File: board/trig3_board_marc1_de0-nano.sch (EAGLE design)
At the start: 305 parts, among them IC1 ICL7660CPA, IC2 ICL7660CPA, IC3 ICL7660CPA, IC4 ICL7660CPA, J10 2p-2.54, J11 2p-2.54, J12 4p-2.54, J13 BU-SMB-V, J131 4p-2.54, J14 BU-SMB-V, J141 2p-2.54, J15 2p-2.54, J16 2p-2.54, J17 2p-2.54, J18 2p-2.54, J19 6HE-160-VG64AC, J20 4p-2.54, J21 4p-2.54, J22 2p-2.54, J23 2p-2.54, J24 2p-2.54, J25 2p-2.54, J26 4p-2.54, J27 4p-2.54, J28 2p-2.54, J29 2p-2.54, J3 4p-2.54, J30 2p-2.54, J31 2p-2.54, J311 4p-2.54, J32 2p-2.54, J33 2p-2.54, J34 2p-2.54, J35 2p-2.54, J36 2p-2.54, J37 2p-2.54, J38 2p-2.54, J39 2p-2.54, J4 2p-2.54, J40 2p-2.54, J41 2p-2.54, J42 2p-2.54, J43 2p-2.54, J48 2p-2.54, J49 2p-2.54, J5 2p-2.54, J50 2p-2.54, J51 2p-2.54, J52 2p-2.54, J53 2p-2.54, J54 2p-2.54, J55 2p-2.54, J6 2p-2.54, J7 4p-2.54, J8 2p-2.54, J9 2p-2.54, K15_R10P BU-SMB-V, K16_R10N BU-SMB-V, M16CLK_3N BU-SMB-V, P11 BU-SMB-V, P14_CLKOUT_4P BU-SMB-V, P15 BU-SMB-V, P16_R15N BU-SMB-V, P9 BU-SMB-V, T10_B16N BU-SMB-V, T12_B18N BU-SMB-V, T13_B20N BU-SMB-V, T14_B23P BU-SMB-V, T15_B23N BU-SMB-V, T9CLK_7N BU-SMB-V

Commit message: slim it down and add usb-serial
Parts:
- removed A12_T21N, A14_CLKOUT_2N, A2_T2N, A3_T2P, A5, A7_T9N, A8CLK_4N, B11, B12_T21P, B16, B5, B7_T9P, B8CLK_4P, C11, C14, C15, C16, C3_CLKOUT_3N, C6, C8, C9_T15N, D11, D14, D15, D16, D3_CLKOUT_3P, D5, D6, D8, D9_T15P, E10, E11, E15CLK_2P, E16CLK_2N, E6, E7, E8_T10N, E9, F14, F15, F16, F8_T10P, F9, G15_R5P, G16_R5N, J13, J14, K15_R10P, K16_R10N, L16_R11N, M16CLK_3N, N12, N14, N15_R13P, N16_R13N, P11, P14_CLKOUT_4P, P15, R10_B16P, R12_B18P, R13_B20P, R14_CLKOUT_4N, T10_B16N, T12_B18N, T13_B20N, T14_B23P, T15_B23N: BU-SMB-V, con-coax:BU-SMB-V
- removed C1, C12, C13, C17, C18, C3, C7, C9: 10uF, SparkFun-Capacitors:CAPPTH1
- removed C19, C2, C20, C21, C22, C4, C5, C91, C93, C94, C95, C97: 0.1uF, SparkFun-Capacitors:CAP0805
- removed IC1, IC2, IC3, IC4: ICL7660CPA, maxim:ICL7660CPA
- removed J1, J2: (no value), SparkFun-Connectors:M13X22X13
- removed J10, J11, J141, J15, J16, J17, J18, J22, J23, J24, J25, J28, J29, J30, J31, J32, J33, J35, J36, J37, J38, J39, J4, J40, J41, J48, J49, J50, J51, J52, J53, J54, J55, J8, J9, OJ1, OJ10, OJ11, OJ12, OJ17, OJ18, OJ19, OJ2, OJ20, OJ21, OJ22, OJ23, OJ24, OJ25, OJ26, OJ27, OJ28, OJ29, OJ3, OJ30, OJ31, OJ32, OJ33, OJ34, OJ35, OJ36, OJ37, OJ38, OJ39, OJ4, OJ40, OJ49, OJ5, OJ50, OJ51, OJ52, OJ53, OJ54, OJ55, OJ56, OJ57, OJ58, OJ59, OJ6, OJ60, OJ61, OJ62, OJ63, OJ64, OJ65, OJ66, OJ67, OJ68, OJ69, OJ7, OJ70, OJ71, OJ72, OJ73, OJ74, OJ75, OJ76, OJ77, OJ78, OJ79, OJ8, OJ80, OJ9: 2p-2.54, Seeed-Connector:DIP-BLACK-MALE-HEADER-VERT(2P-2.54)
- removed J131, J311: 4p-2.54, Seeed-Connector:DIP-BLACK-FEMALE-HEADER-VERT(4P-2.54)
- removed J19: 6HE-160-VG64AC, 19inch:6HE-160-VG64AC
- removed J20, J21, J26, J27: 4p-2.54, Seeed-Connector:DIP-BLACK-MALE-HEADER-VERT(4P-2.54)
- removed R10, R12, R13, R14: 1k, SparkFun-Passives:RESISTORAXIAL-0.3
- removed R100, R11, R111, R141, R15, R161, R18, R19, R20, R21, R22, R23, R24, R25, R26, R27, R28, R29, R30, R32, R33, R35, R39, R4, R40, R45, R46, R47, R49, R50, R51, R52, R53, R9, R91: 50, SparkFun-Passives:RESISTORAXIAL-0.3
- removed R17: 10k, SparkFun-Passives:RESISTORAXIAL-0.3
- removed R2, R3, R7: 3296W 5k, resistor:R-TRIMM3296W
- removed VSLUE, VSLUE2, VSLUE3, VSLUE4, VSLUE6, VSLUE7, VSLUE8, VSLUE9: SN74ACT244DW, SN74ACT244DW:SN74ACT244DW
- added C_OSC1, C_OSC2: 22pF, rcl@1:C-USC0603
- added U340G: CH340G, usb-serial:CH340G
- added USB1: MF-CON-MICROUSB-RIGHT, PP_Connectors:USB_5PIN_10118193-0001LF
- added Y1: ABL-12.000MHZ-B2, SparkFun-FreqCtrl:CRYSTALHC49US
- R1: value 3296W 5k -> 10k; device resistor:R-TRIMM3296W -> adafruit:R-US_R0805
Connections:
- removed net -3V3_1: C3.1, IC1.VOUT, J20.P$1, R10.2
- removed net -3V3_2: C9.1, IC2.VOUT, J21.P$1, R12.2
- removed net -3V3_3: C13.1, IC3.VOUT, J26.P$1, R13.2
- removed net -3V3_4: C18.1, IC4.VOUT, J27.P$1, R14.2
- removed net -V1: C19.2, J20.P$2, OJ9.1, R1.S
- removed net -V2: C20.2, J21.P$2, OJ10.1, R2.S
- removed net -V3: C21.2, J26.P$2, OJ11.1, R3.S
- removed net -V4: C22.2, J27.P$2, OJ12.1, R7.S
- removed net AIN0: J1.24, J131.P$4
- removed net AIN1: J1.25, J311.P$1
- removed net AIN2: J1.22, J131.P$3
- removed net AIN3: J1.21, J311.P$3
- removed net AIN4: J1.23, J311.P$2
- removed net AIN5: J1.18, J131.P$1
- removed net AIN6: J1.19, J311.P$4
- removed net AIN7: J1.20, J131.P$2
- removed net GPIO_018_E7: OJ64.1, SV1.23, VSLUE7.1A3, VSLUE7.1A4
- removed net GPIO_019_D8: OJ21.1, SV1.24, VSLUE2.2A3, VSLUE2.2A4
- removed net GPIO_01_C3: C3_CLKOUT_3N.1, J30.2, R27.2, SV1.4
- removed net GPIO_021_F8: F8_T10P.1, J18.2, R21.2, SV1.26
- removed net GPIO_022_F9: OJ62.1, SV1.27, VSLUE7.2A1, VSLUE7.2A2
- removed net GPIO_023_E9: OJ24.1, SV1.28, VSLUE2.1A3, VSLUE2.1A4
- removed net GPIO_112_N12: OJ23.1, SV2.17, VSLUE2.1A1, VSLUE2.1A2
- removed net GPIO_120_P15: OJ61.1, SV2.25, VSLUE7.2A3, VSLUE7.2A4
- removed net GPIO_20_A14: A14_CLKOUT_2N.1, J1.5, J31.2, R29.2
- removed net GPIO_210_F14: J1.15, OJ30.1, VSLUE3.2A1, VSLUE3.2A2
- removed net GPIO_211_G16: G16_R5N.1, J1.16, J28.2, R24.2
- removed net GPIO_212_G15: G15_R5P.1, J1.17, J29.2, R26.2
- removed net GPIO_21_B16: J1.6, OJ22.1, VSLUE2.2A1, VSLUE2.2A2
- removed net GPIO_22_C14: J1.7, OJ32.1, VSLUE3.1A3, VSLUE3.1A4
- removed net GPIO_23_C16: J1.8, OJ63.1, VSLUE7.1A1, VSLUE7.1A2
- removed net GPIO_24_C15: J1.9, OJ31.1, VSLUE3.1A1, VSLUE3.1A2
- removed net GPIO_25_D16: J1.10, OJ39.1, VSLUE4.1A1, VSLUE4.1A2
- removed net GPIO_26_D15: J1.11, OJ29.1, VSLUE3.2A3, VSLUE3.2A4
- removed net GPIO_27_D14: J1.12, OJ40.1, VSLUE4.1A3, VSLUE4.1A4
- removed net GPIO_28_F15: J1.13, OJ37.1, VSLUE4.2A3, VSLUE4.2A4
- removed net GPIO_29_F16: J1.14, OJ38.1, VSLUE4.2A1, VSLUE4.2A2
- removed net GPIO_2_IN0_E15CLK: E15CLK_2P.1, J1.2, J16.2, R19.2
- removed net GPIO_2_IN1_E16CLK: E16CLK_2N.1, J1.3, J15.2, R18.2
- removed net GPIO_2_IN2_M16CLK: J1.4, J141.2, M16CLK_3N.1, R15.2
- removed net N$1: C1.1, IC1.CAP+
- removed net N$10: R1.E, R10.1
- removed net N$11: R12.1, R2.E
- removed net N$12: R13.1, R3.E
- removed net N$13: R14.1, R7.E
- removed net N$2: C1.2, IC1.CAP-
- removed net N$3: C12.1, IC3.CAP+
- removed net N$4: C7.1, IC2.CAP+
- removed net N$5: C7.2, IC2.CAP-
- removed net N$6: C12.2, IC3.CAP-
- removed net N$7: C17.1, IC4.CAP+
- removed net N$8: C17.2, IC4.CAP-
- removed net OUT1: J14.1, OJ1.1, VSLUE.1Y1, VSLUE.1Y2
- removed net OUT10: E9.1, OJ19.1, VSLUE2.1Y3, VSLUE2.1Y4
- removed net OUT11: D8.1, OJ17.1, VSLUE2.2Y3, VSLUE2.2Y4
- removed net OUT12: B16.1, OJ18.1, VSLUE2.2Y1, VSLUE2.2Y2
- removed net OUT13: C15.1, OJ28.1, VSLUE3.1Y1, VSLUE3.1Y2
- removed net OUT14: C14.1, OJ27.1, VSLUE3.1Y3, VSLUE3.1Y4
- removed net OUT15: D15.1, OJ25.1, VSLUE3.2Y3, VSLUE3.2Y4
- removed net OUT16: F14.1, OJ26.1, VSLUE3.2Y1, VSLUE3.2Y2
- removed net OUT17: D16.1, OJ36.1, VSLUE4.1Y1, VSLUE4.1Y2
- removed net OUT18: D14.1, OJ35.1, VSLUE4.1Y3, VSLUE4.1Y4
- removed net OUT19: F15.1, OJ33.1, VSLUE4.2Y3, VSLUE4.2Y4
- removed net OUT2: D11.1, OJ2.1, VSLUE.1Y3, VSLUE.1Y4
- removed net OUT20: F16.1, OJ34.1, VSLUE4.2Y1, VSLUE4.2Y2
- removed net OUT25: D6.1, OJ52.1, VSLUE6.1Y1, VSLUE6.1Y2
- removed net OUT26: C6.1, OJ51.1, VSLUE6.1Y3, VSLUE6.1Y4
- removed net OUT27: C8.1, OJ49.1, VSLUE6.2Y3, VSLUE6.2Y4
- removed net OUT28: E6.1, OJ50.1, VSLUE6.2Y1, VSLUE6.2Y2
- removed net OUT29: C16.1, OJ60.1, VSLUE7.1Y1, VSLUE7.1Y2
- removed net OUT3: B11.1, OJ3.1, VSLUE.2Y1, VSLUE.2Y2
- removed net OUT30: E7.1, OJ59.1, VSLUE7.1Y3, VSLUE7.1Y4
- removed net OUT31: OJ57.1, P15.1, VSLUE7.2Y3, VSLUE7.2Y4
- removed net OUT32: F9.1, OJ58.1, VSLUE7.2Y1, VSLUE7.2Y2
- removed net OUT33: B5.1, OJ68.1, VSLUE8.1Y1, VSLUE8.1Y2
- removed net OUT34: A5.1, OJ67.1, VSLUE8.1Y3, VSLUE8.1Y4
- removed net OUT35: D5.1, OJ65.1, VSLUE8.2Y3, VSLUE8.2Y4
- removed net OUT36: N14.1, OJ66.1, VSLUE8.2Y1, VSLUE8.2Y2
- removed net OUT37: E11.1, OJ76.1, VSLUE9.1Y1, VSLUE9.1Y2
- removed net OUT38: OJ75.1, P11.1, VSLUE9.1Y3, VSLUE9.1Y4
- removed net OUT39: J13.1, OJ73.1, VSLUE9.2Y3, VSLUE9.2Y4
- removed net OUT4: E10.1, OJ4.1, VSLUE.2Y3, VSLUE.2Y4
- removed net OUT40: C11.1, OJ74.1, VSLUE9.2Y1, VSLUE9.2Y2
- removed net OUT9: N12.1, OJ20.1, VSLUE2.1Y1, VSLUE2.1Y2
- new net +3V3: U340G.V3, U340G.VCC
- new net DMINUS: U340G.D-, USB1.D-
- new net DPLUS: U340G.D+, USB1.D+
- new net N$23: C_OSC1.1, U340G.XI, Y1.1
- new net N$31: C_OSC2.1, U340G.XO, Y1.2
- net 3V3: no longer IC1.V+, IC2.V+, IC3.V+, IC4.V+, J1.1, J20.P$4, J21.P$4, J26.P$4, J27.P$4
- net 5V: now also R1.2, USB1.5V; no longer C2.2, C4.2, C5.2, C91.2, C93.2, C94.2, C95.2, C97.2, J191-A32.MS, J191-C32.MS, J192-A32.MS, J192-C32.MS, R17.1, VSLUE.VCC, VSLUE2.VCC, VSLUE3.VCC, VSLUE4.VCC, VSLUE6.VCC, VSLUE7.VCC, VSLUE8.VCC, VSLUE9.VCC
- net GND: now also C_OSC1.2, C_OSC2.2, U340G.GND, USB1.GND; no longer A12_T21N.2, A14_CLKOUT_2N.2, A2_T2N.2, A3_T2P.2, A5.2, A7_T9N.2, A8CLK_4N.2, B11.2, B12_T21P.2, B16.2, B5.2, B7_T9P.2, B8CLK_4P.2, C11.2, C13.2, C14.2, C15.2, C16.2, C18.2, C19.1, C2.1, C20.1, C21.1, C22.1, C3.2, C3_CLKOUT_3N.2, C4.1, C5.1, C6.2, C8.2, C9.2, C91.1, C93.1, C94.1, C95.1, C97.1, C9_T15N.2, D11.2, D14.2, D15.2, D16.2, D3_CLKOUT_3P.2, D5.2, D6.2, D8.2, D9_T15P.2, E10.2, E11.2, E15CLK_2P.2, E16CLK_2N.2, E6.2, E7.2, E8_T10N.2, E9.2, F14.2, F15.2, F16.2, F8_T10P.2, F9.2, G15_R5P.2, G16_R5N.2, IC1.GND, IC2.GND, IC3.GND, IC4.GND, J1.26, J10.1, J11.1, J13.2, J14.2, J141.1, J15.1, J16.1, J17.1, J18.1, J191-A9.MS, J191-C9.MS, J192-A9.MS, J192-C9.MS, J20.P$3, J21.P$3, J22.1, J23.1, J24.1, J25.1, J26.P$3, J27.P$3, J28.1, J29.1, J30.1, J31.1, J32.1, J33.1, J35.1, J36.1, J37.1, J38.1, J39.1, J4.1, J40.1, J41.1, J48.1, J49.1, J50.1, J51.1, J52.1, J53.1, J54.1, J55.1, J8.1, J9.1, K15_R10P.2, K16_R10N.2, L16_R11N.2, M16CLK_3N.2, N12.2, N14.2, N15_R13P.2, N16_R13N.2, OJ1.2, OJ17.2, OJ18.2, OJ19.2, OJ2.2, OJ20.2, OJ21.2, OJ22.2, OJ23.2, OJ24.2, OJ25.2, OJ26.2, OJ27.2, OJ28.2, OJ29.2, OJ3.2, OJ30.2, OJ31.2, OJ32.2, OJ33.2, OJ34.2, OJ35.2, OJ36.2, OJ37.2, OJ38.2, OJ39.2, OJ4.2, OJ40.2, OJ49.2, OJ5.2, OJ50.2, OJ51.2, OJ52.2, OJ53.2, OJ54.2, OJ55.2, OJ56.2, OJ57.2, OJ58.2, OJ59.2, OJ6.2, OJ60.2, OJ61.2, OJ62.2, OJ63.2, OJ64.2, OJ65.2, OJ66.2, OJ67.2, OJ68.2, OJ69.2, OJ7.2, OJ70.2, OJ71.2, OJ72.2, OJ73.2, OJ74.2, OJ75.2, OJ76.2, OJ77.2, OJ78.2, OJ79.2, OJ8.2, OJ80.2, P11.2, P14_CLKOUT_4P.2, P15.2, R1.A, R100.1, R10_B16P.2, R11.1, R111.1, R12_B18P.2, R13_B20P.2, R141.1, R14_CLKOUT_4N.2, R15.1, R161.1, R18.1, R19.1, R2.A, R20.1, R21.1, R22.1, R23.1, R24.1, R25.1, R26.1, R27.1, R28.1, R29.1, R3.A, R30.1, R32.1, R33.1, R35.1, R39.1, R4.1, R40.1, R45.1, R46.1, R47.1, R49.1, R50.1, R51.1, R52.1, R53.1, R7.A, R9.1, R91.1, T10_B16N.2, T12_B18N.2, T13_B20N.2, T14_B23P.2, T15_B23N.2, VSLUE.GND, VSLUE2.GND, VSLUE3.GND, VSLUE4.GND, VSLUE6.GND, VSLUE7.GND, VSLUE8.GND, VSLUE9.GND
- net GPIO_00_D3: no longer D3_CLKOUT_3P.1, J50.2, R51.2
- net GPIO_012_B7: no longer B7_T9P.1, J49.2, R50.2
- net GPIO_013_D6: no longer OJ55.1, VSLUE6.1A1, VSLUE6.1A2
- net GPIO_014_A7: no longer A7_T9N.1, J35.2, OJ9.2, R33.2
- net GPIO_015_C6: no longer OJ56.1, VSLUE6.1A3, VSLUE6.1A4
- net GPIO_016_C8: no longer OJ53.1, VSLUE6.2A3, VSLUE6.2A4
- net GPIO_017_E6: no longer OJ54.1, VSLUE6.2A1, VSLUE6.2A2
- net GPIO_020_E8: no longer E8_T10N.1, J41.2, OJ12.2, R40.2
- net GPIO_024_C9: no longer C9_T15N.1, J8.2, R91.2
- net GPIO_025_D9: no longer D9_T15P.1, J11.2, R141.2
- net GPIO_026_E11: no longer OJ79.1, VSLUE9.1A1, VSLUE9.1A2
- net GPIO_027_E10: no longer OJ5.1, VSLUE.2A3, VSLUE.2A4
- net GPIO_028_C11: no longer OJ78.1, VSLUE9.2A1, VSLUE9.2A2
- net GPIO_029_B11: no longer OJ6.1, VSLUE.2A1, VSLUE.2A2
- net GPIO_02_A2: no longer A2_T2N.1, J22.2, R20.2
- net GPIO_030_A12: no longer A12_T21N.1, J36.2, OJ10.2, R9.2
- net GPIO_031_D11: no longer OJ8.1, VSLUE.1A3, VSLUE.1A4
- net GPIO_033_B12: no longer B12_T21P.1, J37.2, R11.2
- net GPIO_03_A3: no longer A3_T2P.1, J25.2, R25.2
- net GPIO_07_B5: no longer OJ71.1, VSLUE8.1A1, VSLUE8.1A2
- net GPIO_08_A5: no longer OJ72.1, VSLUE8.1A3, VSLUE8.1A4
- net GPIO_09_D5: no longer OJ69.1, VSLUE8.2A3, VSLUE8.2A4
- net GPIO_0_IN0_A8CLK: no longer A8CLK_4N.1, J24.2, R23.2
- net GPIO_0_IN1_B8CLK: no longer B8CLK_4P.1, J23.2, R22.2
- net GPIO_110_P11: no longer OJ80.1, VSLUE9.1A3, VSLUE9.1A4
- net GPIO_111_R10: no longer J48.2, R10_B16P.1, R49.2
- net GPIO_114_N9: now also R1.1; no longer R17.2, VSLUE.!1OE, VSLUE.!2OE, VSLUE2.!1OE, VSLUE2.!2OE, VSLUE3.!1OE, VSLUE3.!2OE, VSLUE4.!1OE, VSLUE4.!2OE, VSLUE6.!1OE, VSLUE6.!2OE, VSLUE7.!1OE, VSLUE7.!2OE, VSLUE8.!1OE, VSLUE8.!2OE, VSLUE9.!1OE, VSLUE9.!2OE
- net GPIO_116_L16: no longer J32.2, L16_R11N.1, R28.2
- net GPIO_117_K16: no longer J33.2, K16_R10N.1, R30.2
- net GPIO_11_T15: no longer J40.2, OJ11.2, R39.2, T15_B23N.1
- net GPIO_122_R14: no longer J53.2, R14_CLKOUT_4N.1, R46.2
- net GPIO_123_N16: no longer J55.2, N16_R13N.1, R52.2
- net GPIO_124_N15: no longer J54.2, N15_R13P.1, R47.2
- net GPIO_125_P14: no longer J52.2, P14_CLKOUT_4P.1, R45.2
- net GPIO_126_L14: now also U340G.RX
- net GPIO_127_N14: no longer OJ70.1, VSLUE8.2A1, VSLUE8.2A2
- net GPIO_129_L13: now also U340G.TX
- net GPIO_12_T14: no longer J4.2, R4.2, T14_B23P.1
- net GPIO_131_K15: no longer J39.2, K15_R10P.1, R35.2
- net GPIO_132_J13: no longer OJ77.1, VSLUE9.2A3, VSLUE9.2A4
- net GPIO_133_J14: no longer OJ7.1, VSLUE.1A1, VSLUE.1A2
- net GPIO_13_T13: no longer J38.2, R32.2, T13_B20N.1
- net GPIO_14_R13: no longer J17.2, R13_B20P.1, R161.2
- net GPIO_15_T12: no longer J9.2, R100.2, T12_B18N.1
- net GPIO_16_R12: no longer J10.2, R111.2, R12_B18P.1
- net GPIO_18_T10: no longer J51.2, R53.2, T10_B16N.1
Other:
- moved on the sheet: A4, B3, B4, C10, D12, J12, J3, J7, L15_R11P, LED1, P16_R15N, R16_R15P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

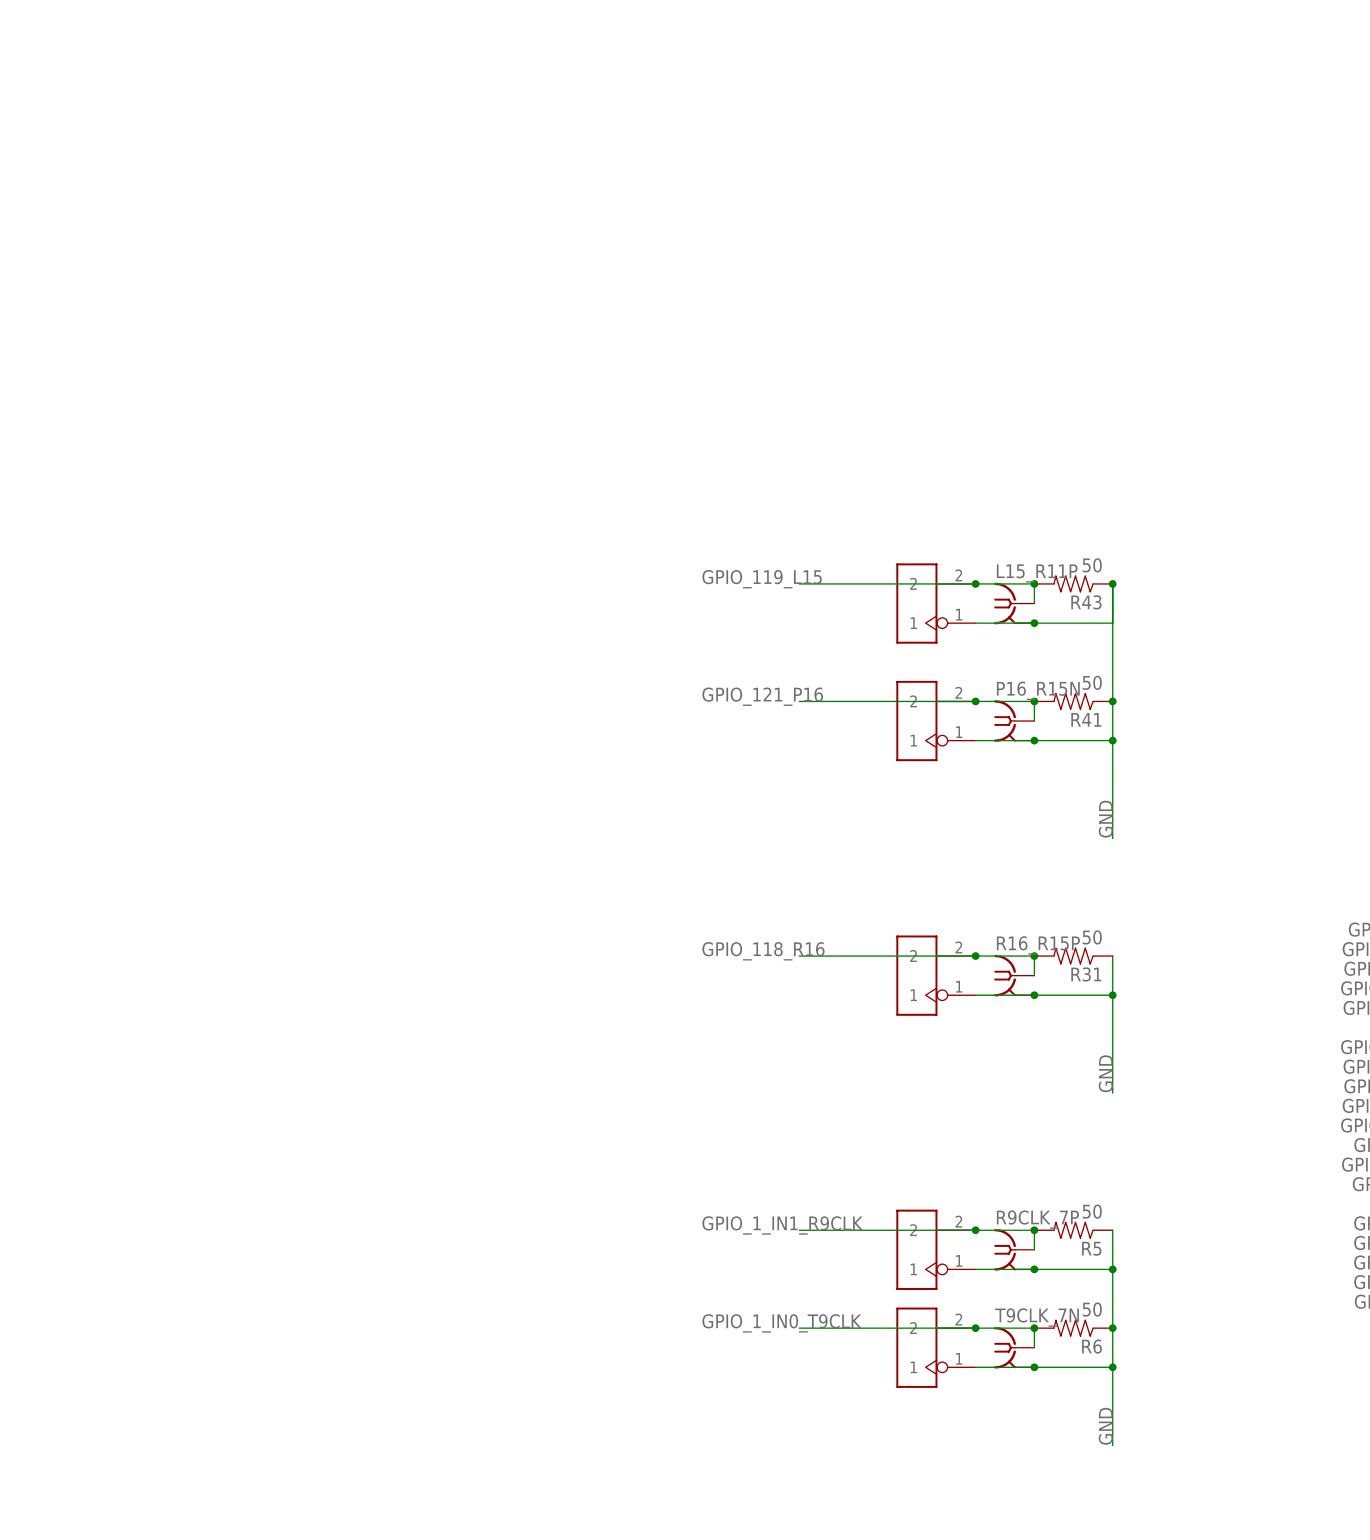
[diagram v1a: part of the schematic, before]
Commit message: updated board schematics: input circuit redesign
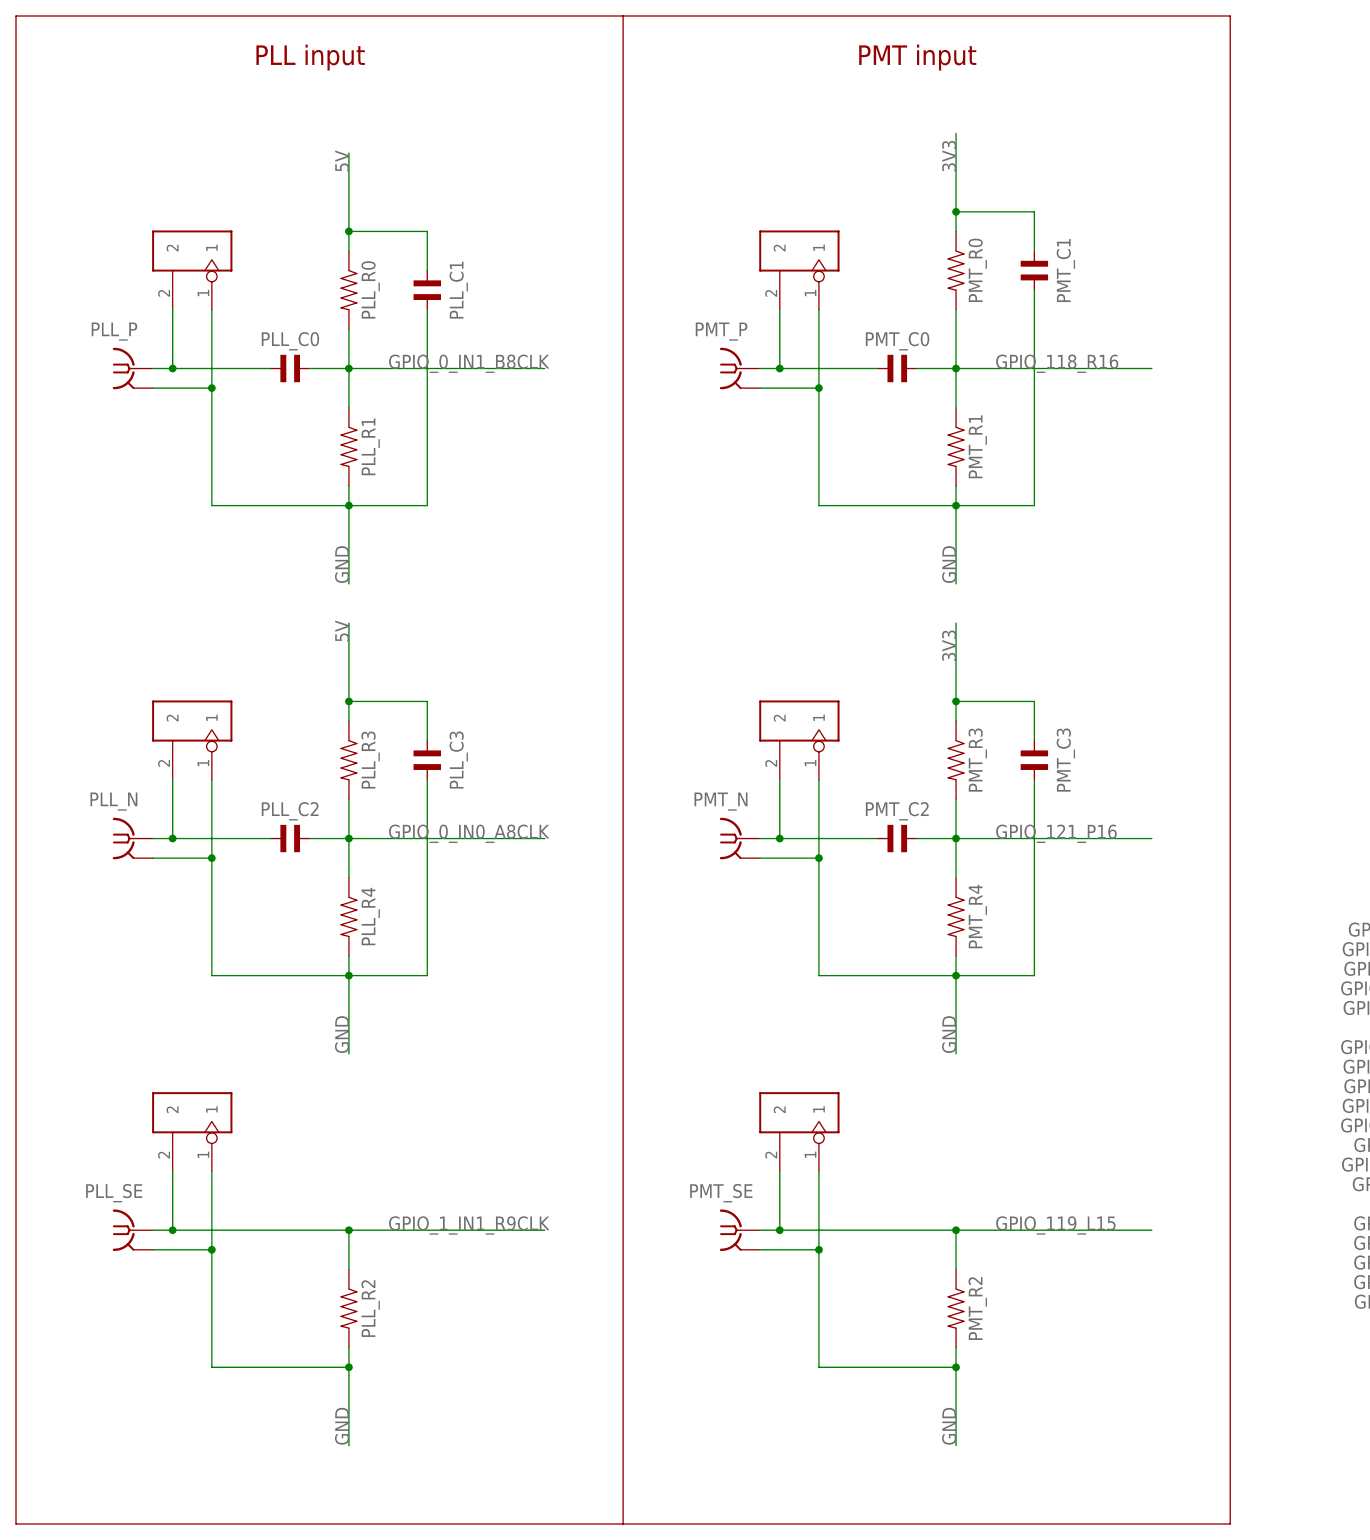
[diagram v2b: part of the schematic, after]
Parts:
- removed J34, J42, J43, J5, J6: 2p-2.54, Seeed-Connector:DIP-BLACK-MALE-HEADER-VERT(2P-2.54)
- removed L15_R11P, P16_R15N, R16_R15P, R9CLK_7P, T9CLK_7N: BU-SMB-V, con-coax:BU-SMB-V
- removed R31, R41, R43, R5, R6: 50, SparkFun-Passives:RESISTORAXIAL-0.3
- added PLL_C0, PLL_C2, PMT_C0, PMT_C2: 1uF, MF_Passives:CAPACITOR_NP_0805
- added PLL_C1, PMT_C1: 0.1uF, MF_Passives:CAPACITOR_NP_0805
- added PLL_C3, PMT_C3: (no value), MF_Passives:CAPACITOR_NP_0805
- added PLL_N, PLL_P, PLL_SE, PMT_N, PMT_P, PMT_SE: BU-SMB-V, con-coax:BU-SMB-V
- added PLL_N_J, PLL_N_J1, PLL_P_J, PMT_N_J, PMT_N_J1, PMT_P_J: 2p-2.54, Seeed-Connector:DIP-BLACK-MALE-HEADER-VERT(2P-2.54)
- added PLL_R0, PLL_R1, PLL_R3, PLL_R4, PMT_R0, PMT_R1, PMT_R3, PMT_R4: (no value), MF_Passives:RESISTOR_0805
- added PLL_R2, PMT_R2: 50ohm, MF_Passives:RESISTOR_0805
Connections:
- new net N$14: PLL_C0.P$1, PLL_P.1, PLL_P_J.2
- new net N$19: PLL_C2.P$1, PLL_N.1, PLL_N_J.2
- new net N$2: PMT_C0.P$1, PMT_P.1, PMT_P_J.2
- new net N$8: PMT_C2.P$1, PMT_N.1, PMT_N_J.2
- net 3V3: now also PMT_C1.P$1, PMT_C3.P$1, PMT_R0.P$1, PMT_R3.P$1
- net 5V: now also PLL_C1.P$1, PLL_C3.P$1, PLL_R0.P$1, PLL_R3.P$1
- net GND: now also PLL_C1.P$2, PLL_C3.P$2, PLL_N.2, PLL_N_J.1, PLL_N_J1.1, PLL_P.2, PLL_P_J.1, PLL_R1.P$2, PLL_R2.P$2, PLL_R4.P$2, PLL_SE.2, PMT_C1.P$2, PMT_C3.P$2, PMT_N.2, PMT_N_J.1, PMT_N_J1.1, PMT_P.2, PMT_P_J.1, PMT_R1.P$2, PMT_R2.P$2, PMT_R4.P$2, PMT_SE.2; no longer J34.1, J42.1, J43.1, J5.1, J6.1, L15_R11P.2, P16_R15N.2, R16_R15P.2, R31.1, R41.1, R43.1, R5.1, R6.1, R9CLK_7P.2, T9CLK_7N.2
- net GPIO_0_IN0_A8CLK: now also PLL_C2.P$2, PLL_R3.P$2, PLL_R4.P$1
- net GPIO_0_IN1_B8CLK: now also PLL_C0.P$2, PLL_R0.P$2, PLL_R1.P$1
- net GPIO_118_R16: now also PMT_C0.P$2, PMT_R0.P$2, PMT_R1.P$1; no longer J34.2, R16_R15P.1, R31.2
- net GPIO_119_L15: now also PMT_N_J1.2, PMT_R2.P$1, PMT_SE.1; no longer J43.2, L15_R11P.1, R43.2
- net GPIO_121_P16: now also PMT_C2.P$2, PMT_R3.P$2, PMT_R4.P$1; no longer J42.2, P16_R15N.1, R41.2
- net GPIO_1_IN0_T9CLK: no longer J6.2, R6.2, T9CLK_7N.1
- net GPIO_1_IN1_R9CLK: now also PLL_N_J1.2, PLL_R2.P$1, PLL_SE.1; no longer J5.2, R5.2, R9CLK_7P.1
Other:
- note added: "PLL input"
- note added: "PMT input"
